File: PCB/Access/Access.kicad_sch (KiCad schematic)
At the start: 69 parts, among them J1 USB-C, J2 RFID, J3 INPUTS, J5 POWER, J6 DOOR2, J7 DOOR1, J8 Shelly, Q2 PMF250XNEX, SW1 ESE13V01D, U1 MD8942, U10 ESP32-S3-MINI-1, U2 MD8942, U3 G3VM-41GR8, U7 QR, U8 G3VM-41GR8, U9 AA

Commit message: Orientation
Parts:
- D1, D2, D3, D4: JLCPCB Rotation Offset 90 -> -90
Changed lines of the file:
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@@
       (effects (font (size 1.27 1.27)) hide)
     )
-    (property "JLCPCB Rotation Offset" "90" (at 121.92 104.14 0)
+    (property "JLCPCB Rotation Offset" "-90" (at 121.92 104.14 0)
       (effects (font (size 1.27 1.27)) hide)
     )
@@
       (effects (font (size 1.27 1.27)) hide)
     )
-    (property "JLCPCB Rotation Offset" "90" (at 121.92 119.38 0)
+    (property "JLCPCB Rotation Offset" "-90" (at 121.92 119.38 0)
       (effects (font (size 1.27 1.27)) hide)
     )
@@
       (effects (font (size 1.27 1.27)) hide)
     )
-    (property "JLCPCB Rotation Offset" "90" (at 121.92 89.535 0)
+    (property "JLCPCB Rotation Offset" "-90" (at 121.92 89.535 0)
       (effects (font (size 1.27 1.27)) hide)
     )
@@
       (effects (font (size 1.27 1.27)) hide)
     )
-    (property "JLCPCB Rotation Offset" "90" (at 121.92 134.62 0)
+    (property "JLCPCB Rotation Offset" "-90" (at 121.92 134.62 0)
       (effects (font (size 1.27 1.27)) hide)
     )
@@
       (effects (font (size 1.27 1.27)) hide)
     )
-    (property "JLCPCB Rotation Offset" "90" (at 121.92 149.86 0)
+    (property "JLCPCB Rotation Offset" "-90" (at 121.92 149.86 0)
       (effects (font (size 1.27 1.27)) hide)
     )
@@
       (effects (font (size 1.27 1.27)) hide)
     )
-    (property "JLCPCB Rotation Offset" "90" (at 122.555 165.1 0)
+    (property "JLCPCB Rotation Offset" "-90" (at 122.555 165.1 0)
       (effects (font (size 1.27 1.27)) hide)
     )
@@
       (effects (font (size 1.27 1.27)) hide)
     )
-    (property "JLCPCB Rotation Offset" "90" (at 122.555 180.34 0)
-      (effects (font (size 1.27 1.27)) hide)
-    )
+    (property "JLCPCB Rotation Offset" "-90" (at 122.555 180.34 0)
+      (effects (font (size 1.27 1.27)) hide)
+    )

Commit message: Smaller
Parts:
- removed D2: D, RevK:D_SOD-123, symbol Device:D
- removed JP1, JP2: 12V, Jumper:SolderJumper-2_P1.3mm_Open_RoundedPad1.0x1.5mm, symbol Jumper:Jumper_2_Open
- J5: footprint RevK:PTSM-HH1-2-RA -> RevK:PTSM-HH1-2-RA-W
- J6: footprint RevK:PTSM-HH1-3-RA-W -> RevK:PTSM-HH1-2-RA; symbol Connector_Generic:Conn_01x03 -> Connector_Generic:Conn_01x02
- J7: footprint RevK:PTSM-HH1-3-RA -> RevK:PTSM-HH1-2-RA; symbol Connector_Generic:Conn_01x03 -> Connector_Generic:Conn_01x02
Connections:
- net DC is gone; now on net +12V: J5.2 (DC)
- net GND: no longer J6.1 (Pin_1), J7.1 (Pin_1)
- net TAMPER: now also U10.15 (GPIO11); no longer U10.8 (GPIO4)
- net at U3.3: now also J6.1 (Pin_1); no longer J6.2 (Pin_2)
- net at U3.4: now also J6.2 (Pin_2); no longer J6.3 (Pin_3)
- net at U8.3: now also J7.1 (Pin_1); no longer J7.2 (Pin_2)
- net at U8.4: now also J7.2 (Pin_2); no longer J7.3 (Pin_3)

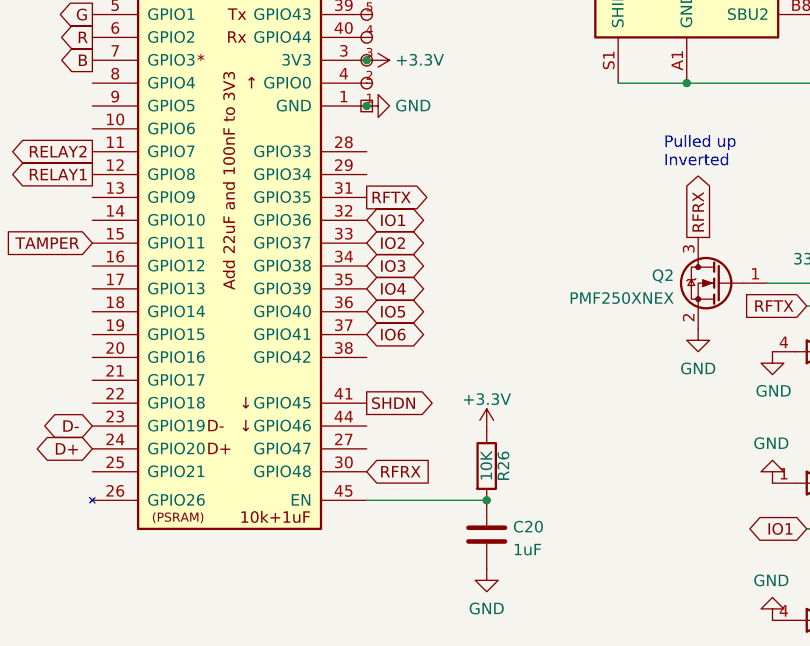
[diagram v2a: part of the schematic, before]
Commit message: Moved GPIO off 48
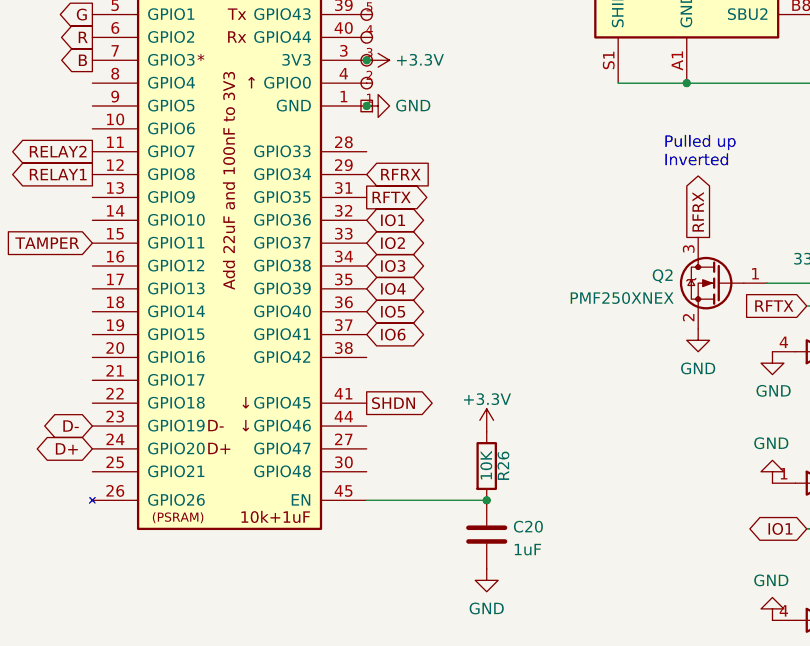
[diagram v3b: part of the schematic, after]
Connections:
- net RFRX: now also U10.29 (GPIO34); no longer U10.30 (GPIO48)
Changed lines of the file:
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@@
     )
   )
-  (global_label "RFRX" (shape input) (at 69.215 102.87 0) (fields_autoplaced)
+  (global_label "RFRX" (shape input) (at 69.215 69.85 0) (fields_autoplaced)
     (effects (font (size 1.27 1.27)) (justify left))
-    (property "Intersheetrefs" "${INTERSHEET_REFS}" (at 76.3047 102.87 0)
+    (property "Intersheetrefs" "${INTERSHEET_REFS}" (at 76.3047 69.85 0)
       (effects (font (size 1.27 1.27)) (justify left) hide)
     )

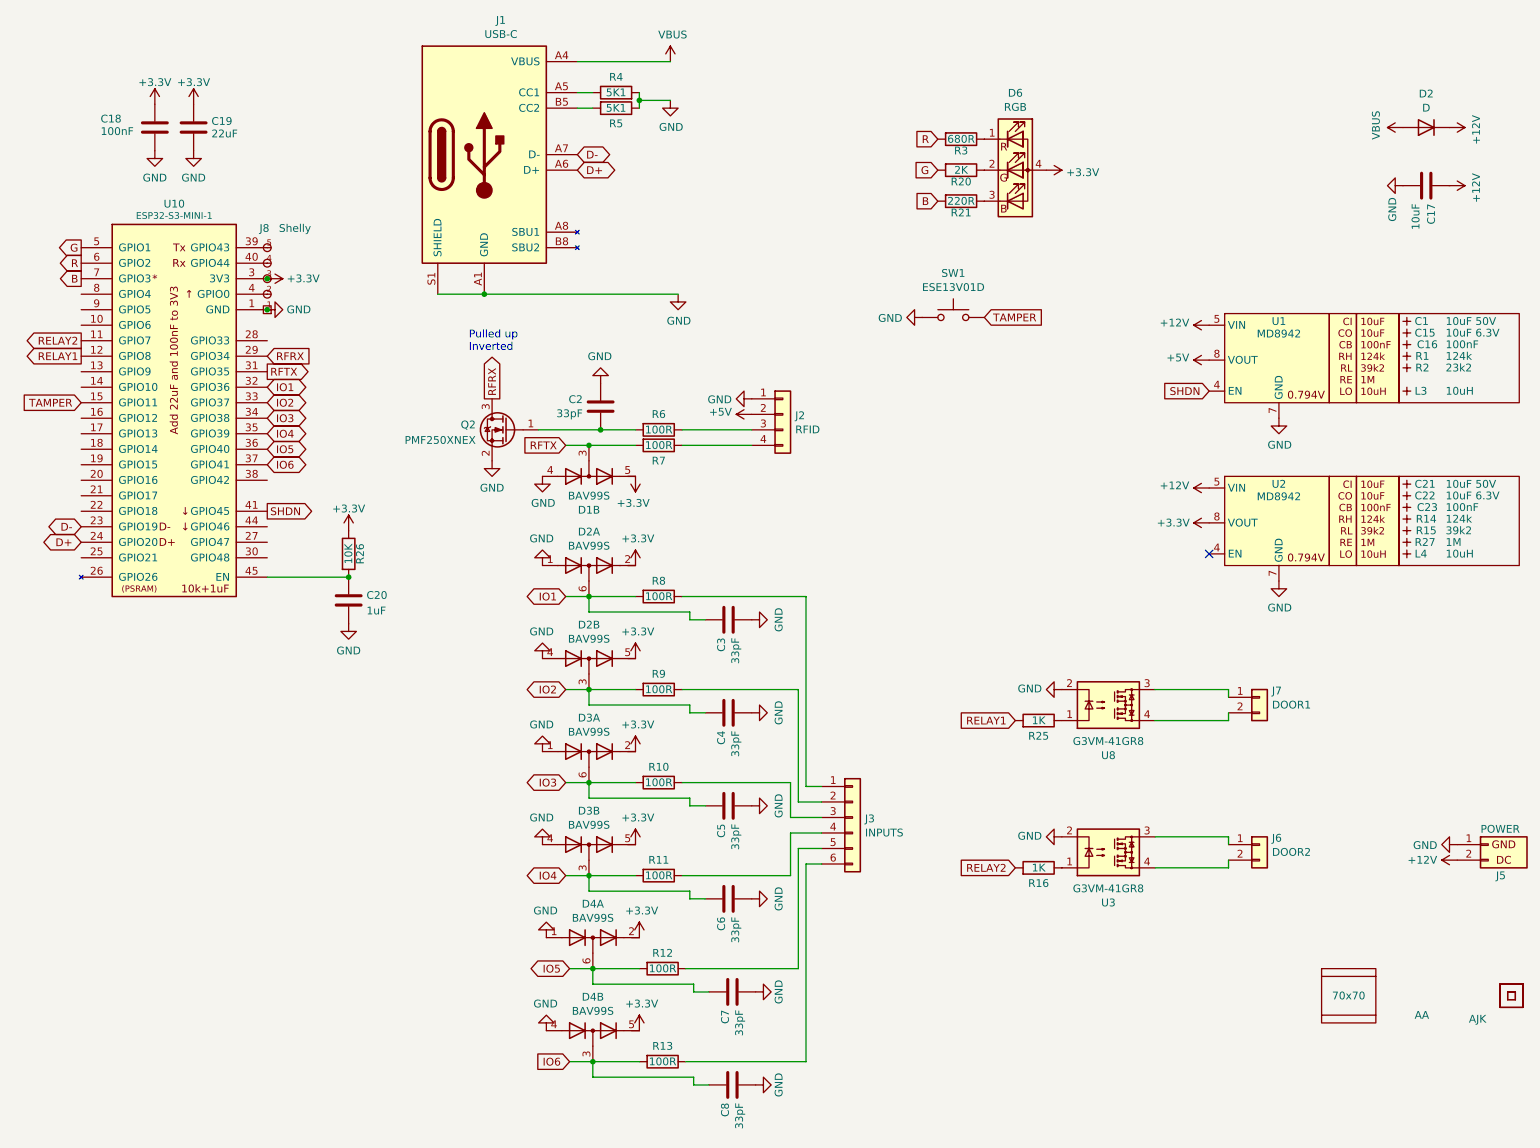
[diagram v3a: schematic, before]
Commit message: USB prog added
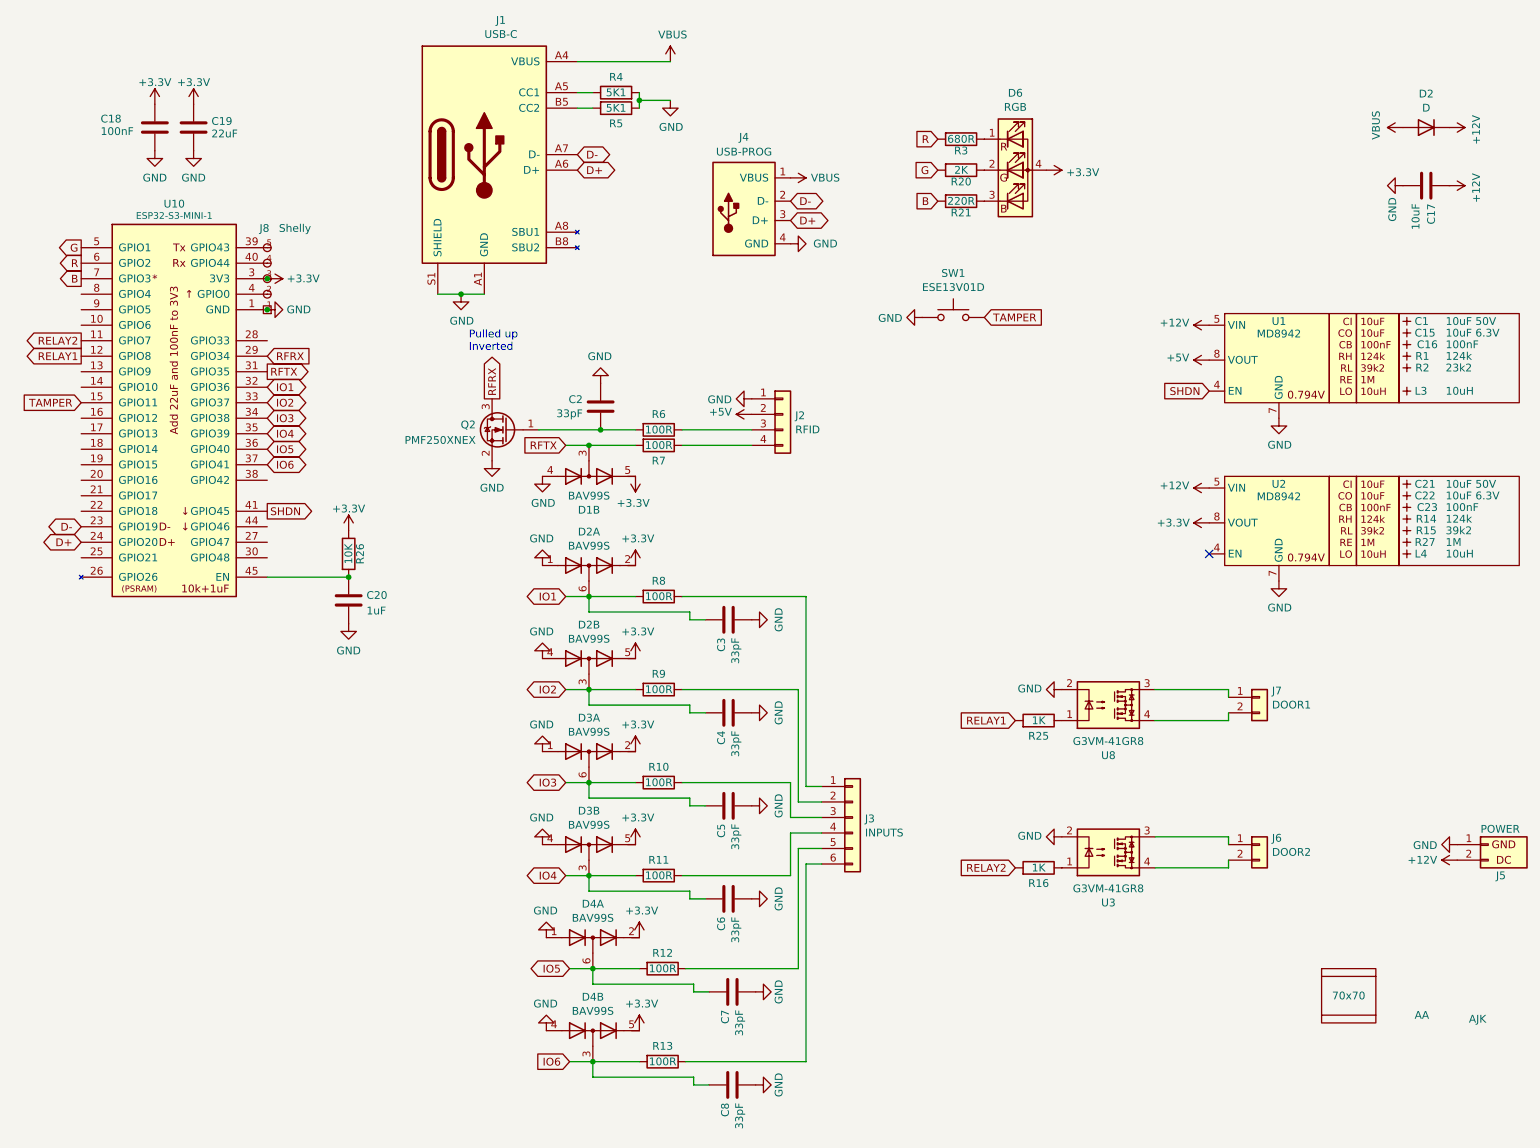
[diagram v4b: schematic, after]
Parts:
- removed U7: QR, RevK:QR-SS, symbol RevK:QR
- added J4: USB-PROG, RevK:USB-PROG, symbol RevK:USB-PROG
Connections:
- net D+: now also J4.3 (D+)
- net D-: now also J4.2 (D-)
- net GND: now also J4.4 (GND)
- net VBUS: now also J4.1 (VBUS)
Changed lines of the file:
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@@
   (junction (at 122.555 170.18) (diameter 0) (color 0 0 0 0)
   )
-  (junction (at 104.775 59.69) (diameter 0) (color 0 0 0 0)
+  (junction (at 100.965 59.69) (diameter 0) (color 0 0 0 0)
   )
   (junction (at 69.215 57.15) (diameter 0) (color 0 0 0 0)
@@
     (stroke (width 0) (type default))
   )
-  (wire (pts (xy 104.775 59.69) (xy 136.525 59.69))
-    (stroke (width 0) (type default))
-  )
   (wire (pts (xy 226.695 129.54) (xy 214.63 129.54))
     (stroke (width 0) (type default))
@@
     (stroke (width 0) (type default))
   )
-  (wire (pts (xy 97.155 59.69) (xy 104.775 59.69))
+  (wire (pts (xy 100.965 59.69) (xy 104.775 59.69))
+    (stroke (width 0) (type default))
+  )
+  (wire (pts (xy 97.155 59.69) (xy 100.965 59.69))
     (stroke (width 0) (type default))
   )
@@
     )
   )
+  (global_label "D+" (shape bidirectional) (at 154.94 47.625 0) (fields_autoplaced)
+    (effects (font (size 1.27 1.27)) (justify left))
+    (property "Intersheetrefs" "${INTERSHEET_REFS}" (at 160.9865 47.625 0)
+      (effects (font (size 1.27 1.27)) (justify left) hide)
+    )
+  )
   (global_label "IO1" (shape bidirectional) (at 69.215 74.93 0) (fields_autoplaced)
     (effects (font (size 1.27 1.27)) (justify left))
@@
     )
   )
+  (global_label "D-" (shape bidirectional) (at 154.94 44.45 0) (fields_autoplaced)
+    (effects (font (size 1.27 1.27)) (justify left))
+    (property "Intersheetrefs" "${INTERSHEET_REFS}" (at 160.9865 44.45 0)
+      (effects (font (size 1.27 1.27)) (justify left) hide)
+    )
+  )
   (global_label "IO3" (shape bidirectional) (at 69.215 80.01 0) (fields_autoplaced)
     (effects (font (size 1.27 1.27)) (justify left))
@@
     )
   )
-  (symbol (lib_id "power:GND") (at 136.525 59.69 0) (unit 1)
+  (symbol (lib_id "power:GND") (at 100.965 59.69 0) (unit 1)
     (in_bom yes) (on_board yes) (dnp no)
-    (property "Reference" "#PWR032" (at 136.525 66.04 0)
+    (property "Reference" "#PWR032" (at 100.965 66.04 0)
       (effects (font (size 1.27 1.27)) hide)
     )
-    (property "Value" "GND" (at 136.652 64.0842 0)
+    (property "Value" "GND" (at 101.092 64.0842 0)
       (effects (font (size 1.27 1.27)))
     )
-    (property "Footprint" "" (at 136.525 59.69 0)
+    (property "Footprint" "" (at 100.965 59.69 0)
       (effects (font (size 1.27 1.27)) hide)
     )
-    (property "Datasheet" "" (at 136.525 59.69 0)
+    (property "Datasheet" "" (at 100.965 59.69 0)
       (effects (font (size 1.27 1.27)) hide)
     )
@@
     )
   )
-  (symbol (lib_id "RevK:QR") (at 273.05 174.625 0) (unit 1)
-    (in_bom no) (on_board yes) (dnp no)
-    (property "Reference" "U7" (at 273.05 177.8 0)
-      (effects (font (size 1.27 1.27)) hide)
-    )
-    (property "Value" "QR" (at 273.05 177.8 0)
-      (effects (font (size 1.27 1.27)) hide)
-    )
-    (property "Footprint" "RevK:QR-SS" (at 272.415 175.26 0)
-      (effects (font (size 1.27 1.27)) hide)
-    )
-    (property "Datasheet" "" (at 272.415 175.26 0)
-      (effects (font (size 1.27 1.27)) hide)
-    )
-    (property "Note" "Non part, PCB printed" (at 273.05 174.625 0)
-      (effects (font (size 1.27 1.27)) hide)
-    )
-    (instances
-      (project "Access"
-        (path "/2a267270-6585-45e3-a633-b53049f10066"
-          (reference "U7") (unit 1)
-        )
-      )
-    )
-  )
   (symbol (lib_id "Switch:SW_Push") (at 181.61 63.5 0) (unit 1)
     (in_bom yes) (on_board yes) (dnp no)
@@
     )
   )
+  (symbol (lib_id "RevK:USB-PROG") (at 147.32 45.72 0) (unit 1)
+    (in_bom yes) (on_board yes) (dnp no) (fields_autoplaced)
+    (property "Reference" "J4" (at 147.32 33.9557 0)
+      (effects (font (size 1.27 1.27)))
+    )
+    (property "Value" "USB-PROG" (at 147.32 36.3799 0)
+      (effects (font (size 1.27 1.27)))
+    )
+    (property "Footprint" "RevK:USB-PROG" (at 151.13 46.99 0)
+      (effects (font (size 1.27 1.27)) hide)
+    )
+    (property "Datasheet" " ~" (at 151.13 46.99 0)
+      (effects (font (size 1.27 1.27)) hide)
+    )
+    (pin "1")
+    (pin "2")
+    (pin "3")
+    (pin "4")
+    (instances
+      (project "Access"
+        (path "/2a267270-6585-45e3-a633-b53049f10066"
+          (reference "J4") (unit 1)
+        )
+      )
+    )
+  )
+  (symbol (lib_id "power:VBUS") (at 154.94 40.64 270) (unit 1)
+    (in_bom yes) (on_board yes) (dnp no)
+    (property "Reference" "#PWR08" (at 151.13 40.64 0)
+      (effects (font (size 1.27 1.27)) hide)
+    )
+    (property "Value" "VBUS" (at 160.655 40.64 90)
+      (effects (font (size 1.27 1.27)))
+    )
+    (property "Footprint" "" (at 154.94 40.64 0)
+      (effects (font (size 1.27 1.27)) hide)
+    )
+    (property "Datasheet" "" (at 154.94 40.64 0)
+      (effects (font (size 1.27 1.27)) hide)
+    )
+    (pin "1")
+    (instances
+      (project "Access"
+        (path "/2a267270-6585-45e3-a633-b53049f10066"
+          (reference "#PWR08") (unit 1)
+        )
+      )
+    )
+  )
   (symbol (lib_id "RevK:ESP32-S3-MINI-1-N4R2") (at 53.975 78.74 0) (unit 1)
     (in_bom yes) (on_board yes) (dnp no) (fields_autoplaced)
@@
         )
       )
+    )
+  )
+  (symbol (lib_id "power:GND") (at 154.94 51.435 90) (unit 1)
+    (in_bom yes) (on_board yes) (dnp no)
+    (property "Reference" "#PWR09" (at 161.29 51.435 0)
+      (effects (font (size 1.27 1.27)) hide)
+    )
+    (property "Value" "GND" (at 160.655 51.435 90)
+      (effects (font (size 1.27 1.27)))
+    )
+    (property "Footprint" "" (at 154.94 51.435 0)
+      (effects (font (size 1.27 1.27)) hide)
+    )
+    (property "Datasheet" "" (at 154.94 51.435 0)
+      (effects (font (size 1.27 1.27)) hide)
+    )
+    (pin "1")
+    (instances
+      (project "Access"
+        (path "/2a267270-6585-45e3-a633-b53049f10066"
+          (reference "#PWR09") (unit 1)
+        )
+      )

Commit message: New reg
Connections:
- net GND: now also U10.44 (GPIO46)
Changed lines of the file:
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@@
+    )
+  )
+  (symbol (lib_id "power:GND") (at 69.215 97.79 90) (unit 1)
+    (in_bom yes) (on_board yes) (dnp no) (fields_autoplaced)
+    (property "Reference" "#PWR010" (at 75.565 97.79 0)
+      (effects (font (size 1.27 1.27)) hide)
+    )
+    (property "Value" "GND" (at 72.39 97.79 90)
+      (effects (font (size 1.27 1.27)) (justify right))
+    )
+    (property "Footprint" "" (at 69.215 97.79 0)
+      (effects (font (size 1.27 1.27)) hide)
+    )
+    (property "Datasheet" "" (at 69.215 97.79 0)
+      (effects (font (size 1.27 1.27)) hide)
+    )
+    (pin "1")
+    (instances
+      (project "Access"
+        (path "/2a267270-6585-45e3-a633-b53049f10066"
+          (reference "#PWR010") (unit 1)
+        )
+      )
+      (project "USBA"
+        (path "/2d210a96-f81f-42a9-8bf4-1b43c11086f3"
+          (reference "#PWR0105") (unit 1)
+        )
+      )
+      (project "Faikin"
+        (path "/46c350bb-7de4-4e81-aafd-4af55e37aab0"
+          (reference "#PWR015") (unit 1)
+        )
+      )
     )
   )

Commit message: Library update
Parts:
- removed D6: RGB, RevK:LED-RGB-1.6x1.6, symbol Device:LED_RGBA
- removed R20: 2K, RevK:R_0402, symbol Device:R
- removed R21: 220R, RevK:R_0402, symbol Device:R
- removed R3: 680R, RevK:R_0402, symbol Device:R
- added D4: XL-1010RGBC-WS2812B, RevK:SMD1010, symbol RevK:WS2812B-1mm
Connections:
- net +3.3V: now also D4.2 (+)
- net GND: now also D4.3 (-)
- net B: no longer names the net of U10.7 (GPIO3)
- net G renamed LED
- net LED: now also D4.4 (I)
- net R: no longer names the net of U10.6 (GPIO2)
- no-connect marks 1 -> 20
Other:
- moved on the sheet: J4
